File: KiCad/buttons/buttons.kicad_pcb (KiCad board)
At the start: 2 copper layers, 19 parts, among them J1 Barrel_Jack_Switch, J10 Conn_01x02_Pin, J2 Conn_01x03_Pin, J3 Conn_01x04_Pin, J4 Conn_01x05_Pin, J5 Conn_01x06_Pin, J6 Conn_01x07_Pin, J7 Conn_01x08_Pin, J8 Conn_01x09_Pin, J9 Conn_01x10_Pin, SW1 Cherry Switch Single, SW2 Cherry Switch 1.5x - Enter Key, U2 TMC2209, U3 Display, U4 ICM-20948, U5 24LC512, U6 Adafruit_ICM20948, U7 LTV-817S

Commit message: PCB designs started
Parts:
- removed J10: Conn_01x02_Pin, Connector_JST:JST_PH_B2B-PH-K_1x02_P2.00mm_Vertical
- removed J2: Conn_01x03_Pin, Connector_JST:JST_PH_B3B-PH-K_1x03_P2.00mm_Vertical
- removed J3: Conn_01x04_Pin, Connector_JST:JST_PH_B4B-PH-K_1x04_P2.00mm_Vertical
- removed J4: Conn_01x05_Pin, Connector_JST:JST_PH_B5B-PH-K_1x05_P2.00mm_Vertical
- removed J5: Conn_01x06_Pin, Connector_JST:JST_PH_B6B-PH-K_1x06_P2.00mm_Vertical
- removed J6: Conn_01x07_Pin, Connector_JST:JST_PH_B7B-PH-K_1x07_P2.00mm_Vertical
- removed J7: Conn_01x08_Pin, Connector_JST:JST_PH_B8B-PH-K_1x08_P2.00mm_Vertical
- removed J8: Conn_01x09_Pin, Connector_JST:JST_PH_B9B-PH-K_1x09_P2.00mm_Vertical
- removed J9: Conn_01x10_Pin, Connector_JST:JST_PH_B10B-PH-K_1x10_P2.00mm_Vertical
- removed U1: ~, ComponentLib:NUCLEO-F767ZI
- removed U2: TMC2209, ComponentLib:TMC2209 Silentstepstick
- removed U3: Display, ComponentLib:NHD-2.23-12832UCB3
- removed U4: ICM-20948, ComponentLib:ICM-20948
- removed U5: 24LC512, Package_SO:SOIC-8_5.3x6.2mm_P1.27mm
- removed U6: Adafruit_ICM20948, ComponentLib:Adafruit-ICM-20948
- removed U7: LTV-817S, Package_DIP:SMDIP-4_W9.53mm
- added C1: 100n, Capacitor_SMD:C_0603_1608Metric, B.Cu at (128.7, 99.2)
- added C2: 100n, Capacitor_SMD:C_0603_1608Metric, B.Cu at (148.2, 99.2)
- added C3: 100n, Capacitor_SMD:C_0603_1608Metric, B.Cu at (167.7, 99.2)
- added C4: 100n, Capacitor_SMD:C_0603_1608Metric, B.Cu at (128.7, 118.7)
- added C5: 100n, Capacitor_SMD:C_0603_1608Metric, B.Cu at (148.2, 118.7)
- added C6: 100n, Capacitor_SMD:C_0603_1608Metric, B.Cu at (167.7, 118.7)
- added C7: 100n, Capacitor_SMD:C_0603_1608Metric, B.Cu at (128.7, 138.2)
- added H1: MountingHole, MountingHole:MountingHole_3.2mm_M3, F.Cu at (109.0, 93.5)
- added H2: MountingHole, MountingHole:MountingHole_3.2mm_M3, F.Cu at (172.0, 156.5)
- added H3: MountingHole, MountingHole:MountingHole_3.2mm_M3, F.Cu at (172.0, 93.5)
- added H4: MountingHole, MountingHole:MountingHole_3.2mm_M3, F.Cu at (109.0, 156.5)
- added R1: 1k, Resistor_SMD:R_0603_1608Metric, B.Cu at (128.7, 101.2)
- added R10: 10k, Resistor_SMD:R_0603_1608Metric, B.Cu at (128.7, 116.7)
- added R11: 10k, Resistor_SMD:R_0603_1608Metric, B.Cu at (148.2, 116.7)
- added R12: 10k, Resistor_SMD:R_0603_1608Metric, B.Cu at (167.7, 116.7)
- added R13: 1k, Resistor_SMD:R_0603_1608Metric, B.Cu at (128.7, 140.2)
- added R14: 10k, Resistor_SMD:R_0603_1608Metric, B.Cu at (128.7, 136.2)
- added R2: 1k, Resistor_SMD:R_0603_1608Metric, B.Cu at (148.2, 101.2)
- added R3: 1k, Resistor_SMD:R_0603_1608Metric, B.Cu at (167.7, 101.2)
- added R4: 10k, Resistor_SMD:R_0603_1608Metric, B.Cu at (128.7, 97.2)
- added R5: 10k, Resistor_SMD:R_0603_1608Metric, B.Cu at (148.2, 97.2)
- added R6: 10k, Resistor_SMD:R_0603_1608Metric, B.Cu at (167.7, 97.2)
- added R7: 1k, Resistor_SMD:R_0603_1608Metric, B.Cu at (128.7, 120.7)
- added R8: 1k, Resistor_SMD:R_0603_1608Metric, B.Cu at (148.2, 120.7)
- added R9: 1k, Resistor_SMD:R_0603_1608Metric, B.Cu at (167.7, 120.7)
- added SW3: Cherry Switch Single, ComponentLib:SW_Cherry_MX_1.00u_PCB, F.Cu at (160.0, 105.5)
- added SW4: Cherry Switch Single, ComponentLib:SW_Cherry_MX_1.00u_PCB, F.Cu at (121.0, 125.0)
- added SW5: Cherry Switch Single, ComponentLib:SW_Cherry_MX_1.00u_PCB, F.Cu at (140.5, 125.0)
- added SW6: Cherry Switch Single, ComponentLib:SW_Cherry_MX_1.00u_PCB, F.Cu at (160.0, 125.0)
- added SW7: Cherry Switch Single, ComponentLib:SW_Cherry_MX_1.00u_PCB, F.Cu at (121.0, 144.5)
- J1: value Barrel_Jack_Switch -> Conn_01x09_Pin; footprint Connector_BarrelJack:BarrelJack_Wuerth_694106106102_2.0x5.5mm -> Connector_JST:JST_PH_B9B-PH-K_1x09_P2.00mm_Vertical; moved to B.Cu
- SW2: value Cherry Switch 1.5x - Enter Key -> Cherry Switch Single; footprint ComponentLib:SW_Cherry_MX_1.50u_PCB -> ComponentLib:SW_Cherry_MX_1.00u_PCB
- moved SW2 94.5 mm to (140.5, 105.5)
- moved J1 92.9 mm to (142.8, 152.2)
- moved SW1 85.7 mm to (121.0, 105.5)
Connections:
- J1 pad 1: unconnected-(J1-Pad1) -> +3V3
- J1 pad 2: unconnected-(J1-Pad2) -> /BTN_MEMSLOT
- J1 pad 3: unconnected-(J1-Pad3) -> /BTN_FIX_AX
- SW1 pad 1: unconnected-(SW1-Pad1) -> Net-(R1-Pad1)
- SW1 pad 2: unconnected-(SW1-Pad2) -> +3V3
- SW2 pad 1: unconnected-(SW2-Pad1) -> Net-(R2-Pad1)
- SW2 pad 2: unconnected-(SW2-Pad2) -> +3V3
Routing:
- net +3V3: track 0.00 -> 149.9 mm
- net /BTN_SET: track 0.00 -> 131.0 mm
- net /BTN_FIX_AX: track 0.00 -> 115.6 mm
- net /BTN_MEMSLOT: track 0.00 -> 96.3 mm
- net /BTN_EXTERNAL_EXTRA: track 0.00 -> 47.8 mm
- net /BTN_OK: track 0.00 -> 44.4 mm
- net /BTN_FREE_MOOVE: track 0.00 -> 41.3 mm
- net /BTN_TRACKED_AX: track 0.00 -> 37.1 mm
- net Net-(R8-Pad1): track 0.00 -> 4.66 mm
- net Net-(R3-Pad1): track 0.00 -> 4.65 mm
- net Net-(R9-Pad1): track 0.00 -> 4.64 mm
- net Net-(R13-Pad1): track 0.00 -> 4.63 mm
- net Net-(R7-Pad1): track 0.00 -> 4.63 mm
- net Net-(R1-Pad1): track 0.00 -> 4.63 mm
- net Net-(R2-Pad1): track 0.00 -> 4.61 mm
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- added copper zone on B.Cu, net GND
- added copper zone on F.Cu, net GND
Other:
- board outline added: 73 x 73 mm
- board text added: "3V3"
- board text added: "EXTRA_BTN (SW7)"
- board text added: "FIX_AX (SW2)"
- board text added: "FREE_MOOVE (SW6)"
- board text added: "GND"
- board text added: "MEM_SLOT (SW1)"
- board text added: "OK (SW4)"
- board text added: "SET (SW3)"
- board text added: "SW1 SW2 SW3 SW4 SW5 SW6 SW7"
- board text added: "SW3 SW2 SW1 SW6 SW5 SW4 SW7"
- board text added: "TRACKED_AX (SW5)"

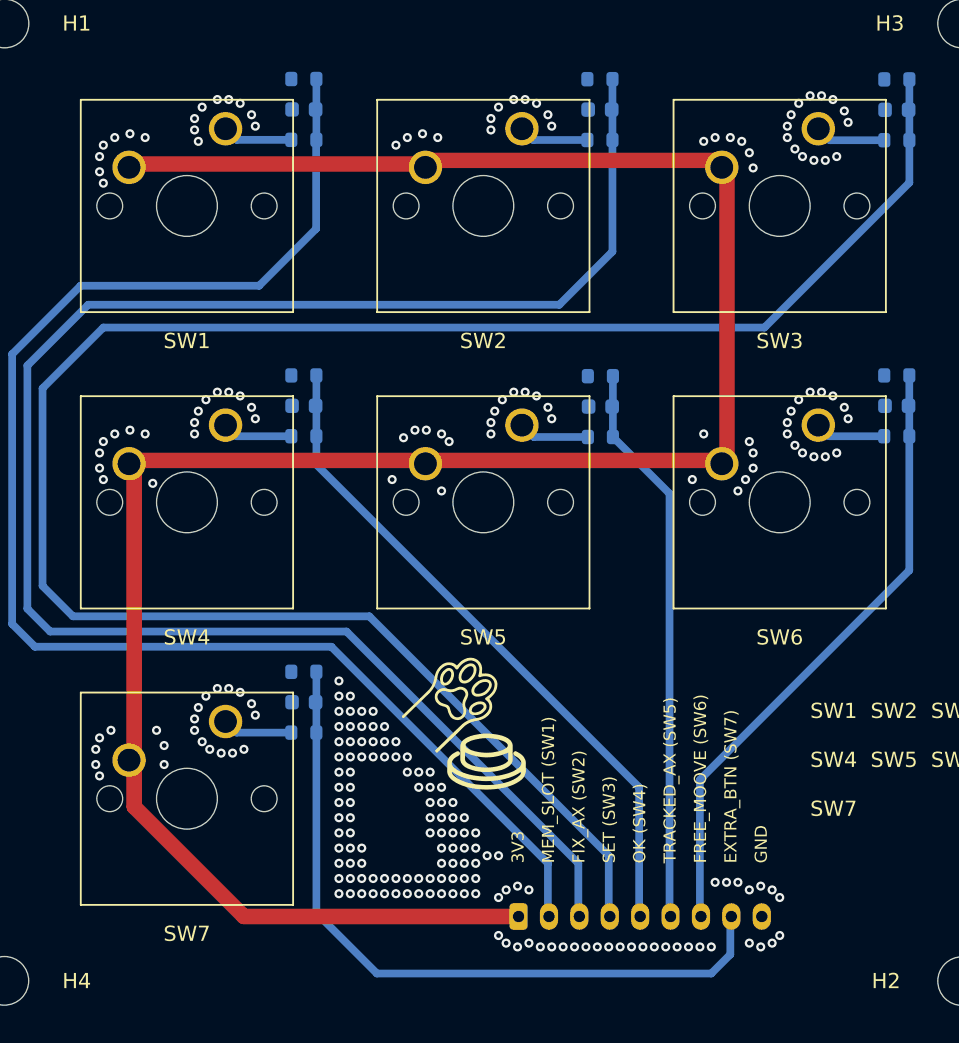
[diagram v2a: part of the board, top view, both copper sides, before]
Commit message: PCB bugfixes based on review
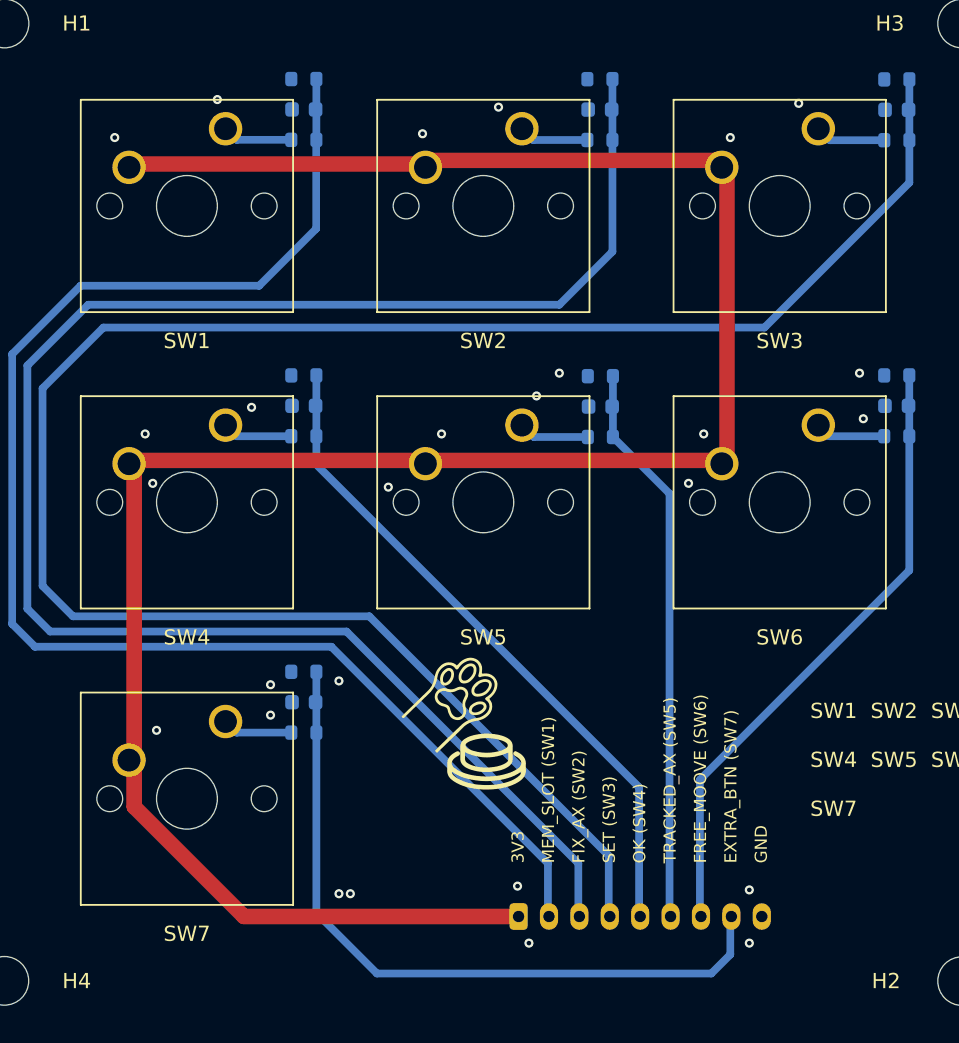
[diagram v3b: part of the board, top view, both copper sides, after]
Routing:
- net +3V3: track 149.9 -> 145.7 mm
- net GND: vias 254 -> 27
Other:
- board text added: "Buttons board Designed by: Sásdi András 2025. Rev. 1"
